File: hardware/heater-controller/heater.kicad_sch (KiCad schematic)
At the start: 15 parts, among them J201 heater LiPo, J202 heater, J203 heater_SW_EX, Q201 Nch, SW201 heater_SW

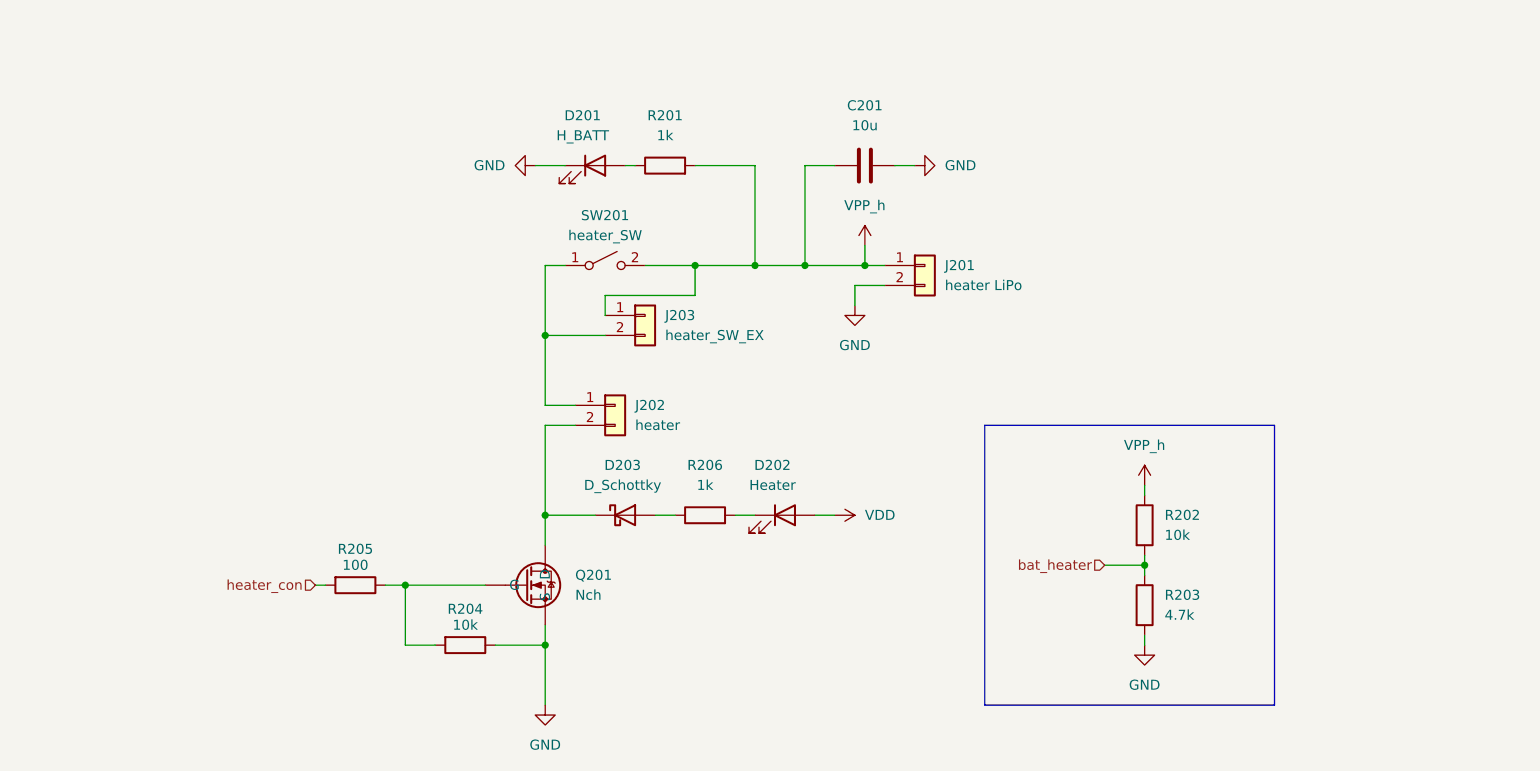
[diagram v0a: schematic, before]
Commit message: BBMで問題がなければ発注可能
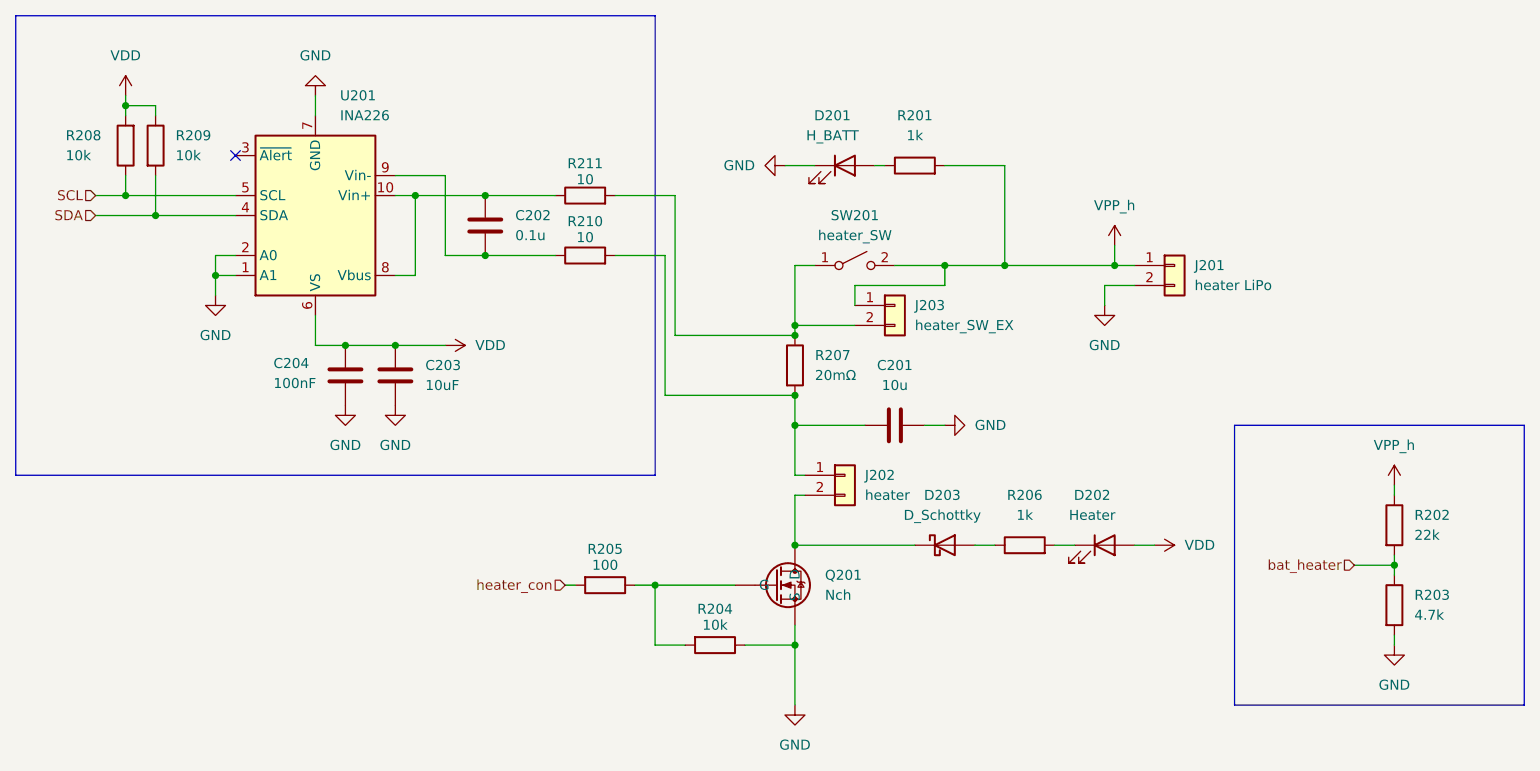
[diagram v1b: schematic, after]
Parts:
- added C202: 0.1u, Capacitor_SMD:C_0805_2012Metric, symbol Device:C
- added C203: 10uF, Capacitor_SMD:C_1206_3216Metric, symbol Device:C
- added C204: 100nF, Capacitor_SMD:C_0805_2012Metric, symbol Device:C
- added R207: 20mΩ, Resistor_SMD:R_2512_6332Metric, symbol Device:R
- added R208, R209: 10k, Resistor_SMD:R_0805_2012Metric, symbol Device:R
- added R210, R211: 10, Resistor_SMD:R_0805_2012Metric, symbol Device:R
- added U201: INA226, Package_SO:VSSOP-10_3x3mm_P0.5mm, symbol Sensor_Energy:INA226
- R202: value 10k -> 22k
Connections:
- net GND: now also C203.2, C204.2, U201.1 (A1), U201.2 (A0), U201.7 (GND)
- net VDD: now also C203.1, C204.1, R208.2, R209.1, U201.6 (VS)
- net VPP_h: no longer C201.2
- net at J203.2 (Pin_2), SW201.1 (A): now also R207.1, R211.2; no longer J202.1 (Pin_1)
- new net: C202.1, R211.1, U201.10 (Vin+), U201.8 (Vbus)
- new net: C202.2, R210.1, U201.9 (Vin-)
- new net: C201.2, J202.1 (Pin_1), R207.2, R210.2
- new net SCL: R208.1, U201.5 (SCL)
- new net SDA: R209.2, U201.4 (SDA)
- no-connect marks 0 -> 1
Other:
- moved on the sheet: C201, D201, D202, D203, J201, J202, J203, Q201, R201, R202, R203, R204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

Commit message: いろいろ
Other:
- note added: "add:0x40"
